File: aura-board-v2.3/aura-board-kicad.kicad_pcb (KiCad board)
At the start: 2 copper layers, 76.8 x 53.3 mm, 21 parts, among them J1 Main Power, J2 PWM_8, J3 BBCON, J4 Atto, J5 GPS, J6 SBUS, J7 Tele, J8 I2C0, U1 TSR2-2450, U2 PocketBeagle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

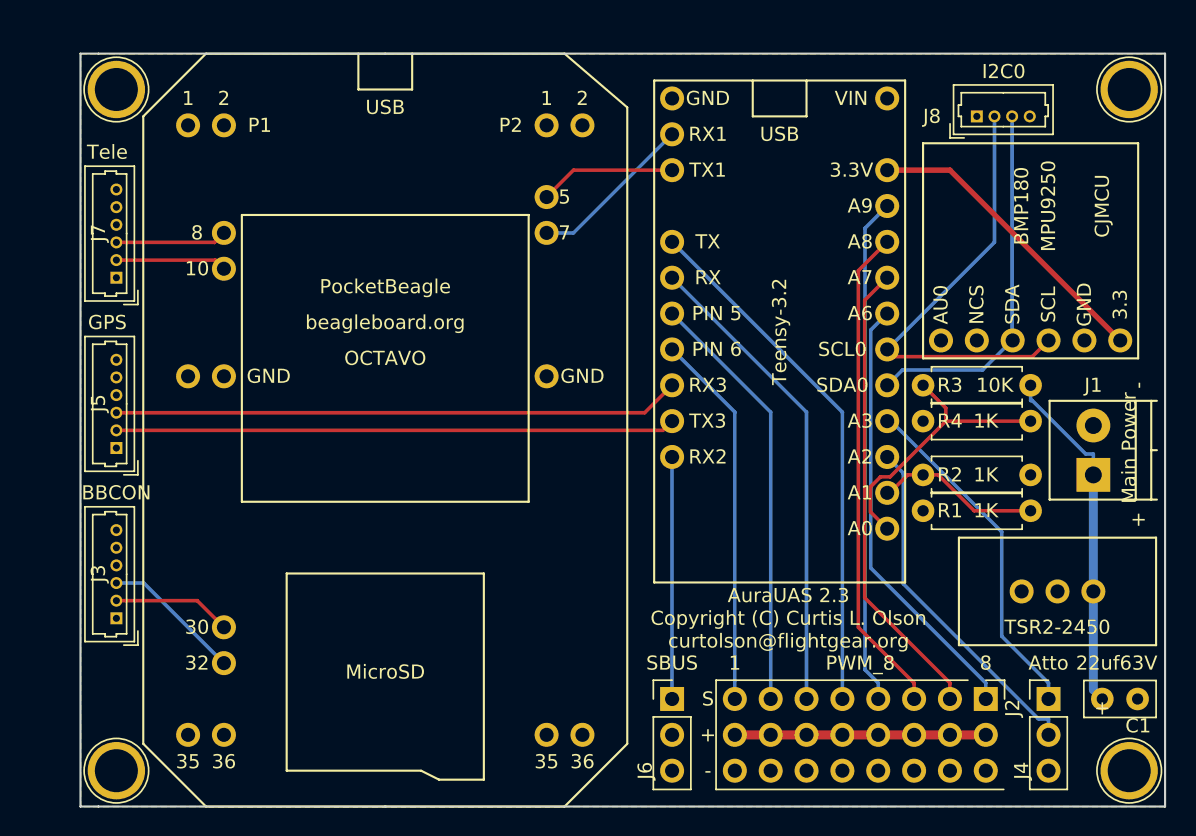
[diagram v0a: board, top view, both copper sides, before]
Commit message: Initial v2.3 design fixes and tweaks: - reverse tx/rx on gps and telemetry (big dohhh!) - slide screw terminal slightly towards board edge - mark pin #1 on TSR2-2450 connector clearly - relocate capacitor - bigger usb port outlines on teensy/pocketbeagle - space sbus and atto connectors exactly 0.2" from ends of PWM block.
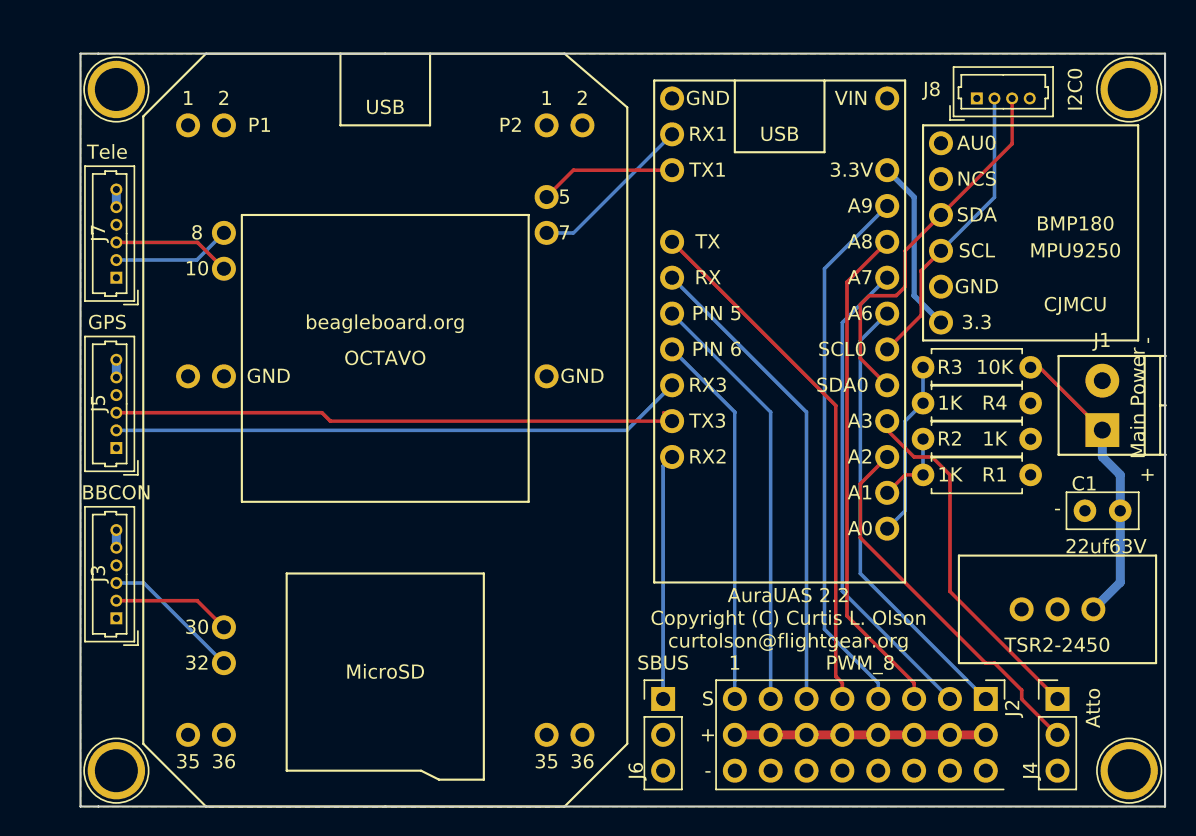
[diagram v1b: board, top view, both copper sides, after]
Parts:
- moved C1 13.4 mm to (101.6, 81.9), turned to 180 degrees
- moved U4 9.92 mm to (95.2, 69.8), turned to 180 degrees
- moved R1 8.03 mm to (87.6, 79.4), turned to 0 degrees
- moved R4 7.73 mm to (95.2, 74.3), turned to 180 degrees
- moved J1 3.24 mm to (100.3, 76.2)
- moved R2 2.54 mm to (95.2, 76.8)
- moved R3 1.27 mm to (87.6, 71.8)
- moved J8 1.27 mm to (91.4, 52.7)
- moved U1 1.27 mm to (97.2, 92.7)
- moved J4 0.64 mm to (97.2, 95.2)
- moved J6 0.63 mm to (69.2, 95.2)
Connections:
- J7 pad 2: /UART2_TX -> /MODEM_TX
- J7 pad 3: /UART2_RX -> /MODEM_RX
- U2 pad 10: /UART2_TX -> /MODEM_RX
- U2 pad 8: /UART2_RX -> /MODEM_TX
- U3 pad 10: /GPS_TX -> /GPS_RX
- U3 pad 9: /GPS_RX -> /GPS_TX
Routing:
- net /I2C0_SCL: track 31.8 -> 20.9 mm
- net +3V3: track 21.5 -> 12.4 mm
- net /MODEM_TX: track 0.00 -> 8.42 mm
- net /MODEM_RX: track 0.00 -> 8.39 mm
- net /UART2_RX: track 7.90 -> 0.00 mm
- net /UART2_TX: track 7.87 -> 0.00 mm
- net /MAIN_VCC: track 19.9 -> 12.5 mm
- net /AVIONICS_VCC: track 11.7 -> 5.61 mm
- net VDD: track 24.7 -> 20.9 mm
- net GND: track 0.00 -> 3.75 mm
- net /PWM5: track 36.0 -> 38.3 mm
- net /ATTO_AMPS: track 24.8 -> 26.6 mm
- net /PWM7: track 33.0 -> 34.3 mm
- net /ATTO_VOLTS: track 24.6 -> 25.7 mm
- net /GPS_TX: track 39.6 -> 40.7 mm
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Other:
- net class Default: clearance 0.1524 -> 0.254
- rule trace_clearance: 0.1524 -> 0.254
- board text added: "AuraUAS 2.2 Copyright (C) Curtis L. Olson curtolson@flightgear.org"
- board text removed: "8"
- board text removed: "AuraUAS 2.3 Copyright (C) Curtis L. Olson curtolson@flightgear.org"

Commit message: Bump up the version number in the board label Fiddle with traces a bit more.
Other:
- board text added: "AuraUAS 2.3 Copyright (C) Curtis L. Olson curtolson@flightgear.org"
- board text removed: "AuraUAS 2.2 Copyright (C) Curtis L. Olson curtolson@flightgear.org"
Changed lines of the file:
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@@
     (area 27.600999 47.993 105.309001 104.459)
     (thickness 1.6)
-    (drawings 14)
+    (drawings 15)
     (tracks 100)
     (zones 0)
@@
   )
   (setup
-    (last_trace_width 0.635)
+    (last_trace_width 0.254)
     (user_trace_width 0.381)
     (user_trace_width 0.508)
@@
       (net 11 +5V))
   )
+  (gr_text 1 (at 101.6 88.9) (layer F.SilkS)
+    (effects (font (size 1 1) (thickness 0.25)))
+  )
   (gr_text - (at 97.155 81.915 180) (layer F.SilkS)
     (effects (font (size 1 1) (thickness 0.25)))
   )
-  (gr_text "AuraUAS 2.2\nCopyright (C) Curtis L. Olson\ncurtolson@flightgear.org" (at 78.105 89.535) (layer F.SilkS)
+  (gr_text "AuraUAS 2.3\nCopyright (C) Curtis L. Olson\ncurtolson@flightgear.org" (at 78.105 89.535) (layer F.SilkS)
     (effects (font (size 1 1) (thickness 0.15)))
   )
@@
   (segment (start 30.48 71.22) (end 30.48 72.47) (width 0.635) (layer B.Cu) (net 2))
   (segment (start 30.48 60.405) (end 30.48 59.155) (width 0.635) (layer B.Cu) (net 2))
-  (segment (start 74.295 74.93) (end 74.295 95.25) (width 0.254) (layer B.Cu) (net 3))
-  (segment (start 69.85 70.485) (end 74.295 74.93) (width 0.254) (layer B.Cu) (net 3))
+  (segment (start 74.295 74.93) (end 74.295 95.25) (width 0.254) (layer B.Cu) (net 3) (status 800000))
+  (segment (start 69.85 70.485) (end 74.295 74.93) (width 0.254) (layer B.Cu) (net 3) (status 400000))
   (segment (start 76.835 74.93) (end 76.835 95.25) (width 0.254) (layer B.Cu) (net 4))
   (segment (start 69.85 67.945) (end 76.835 74.93) (width 0.254) (layer B.Cu) (net 4))
   (segment (start 79.375 74.93) (end 79.375 95.25) (width 0.254) (layer B.Cu) (net 5))
   (segment (start 69.85 65.405) (end 79.375 74.93) (width 0.254) (layer B.Cu) (net 5))
-  (segment (start 81.4469 93.6522) (end 81.915 94.1203) (width 0.254) (layer F.Cu) (net 6))
-  (segment (start 81.4469 74.4619) (end 81.4469 93.6522) (width 0.254) (layer F.Cu) (net 6))
-  (segment (start 69.85 62.865) (end 81.4469 74.4619) (width 0.254) (layer F.Cu) (net 6))
-  (segment (start 81.915 95.25) (end 81.915 94.1203) (width 0.254) (layer F.Cu) (net 6))
+  (segment (start 81.915 95.25) (end 81.915 90.805) (width 0.254) (layer F.Cu) (net 6) (status 400000))
+  (segment (start 81.28 74.295) (end 69.85 62.865) (width 0.254) (layer F.Cu) (net 6) (status 800000))
+  (segment (start 81.28 90.17) (end 81.28 74.295) (width 0.254) (layer F.Cu) (net 6))
+  (segment (start 81.915 90.805) (end 81.28 90.17) (width 0.254) (layer F.Cu) (net 6))
   (segment (start 80.645 90.3103) (end 84.455 94.1203) (width 0.254) (layer B.Cu) (net 7))
   (segment (start 80.645 64.77) (end 80.645 90.3103) (width 0.254) (layer B.Cu) (net 7))

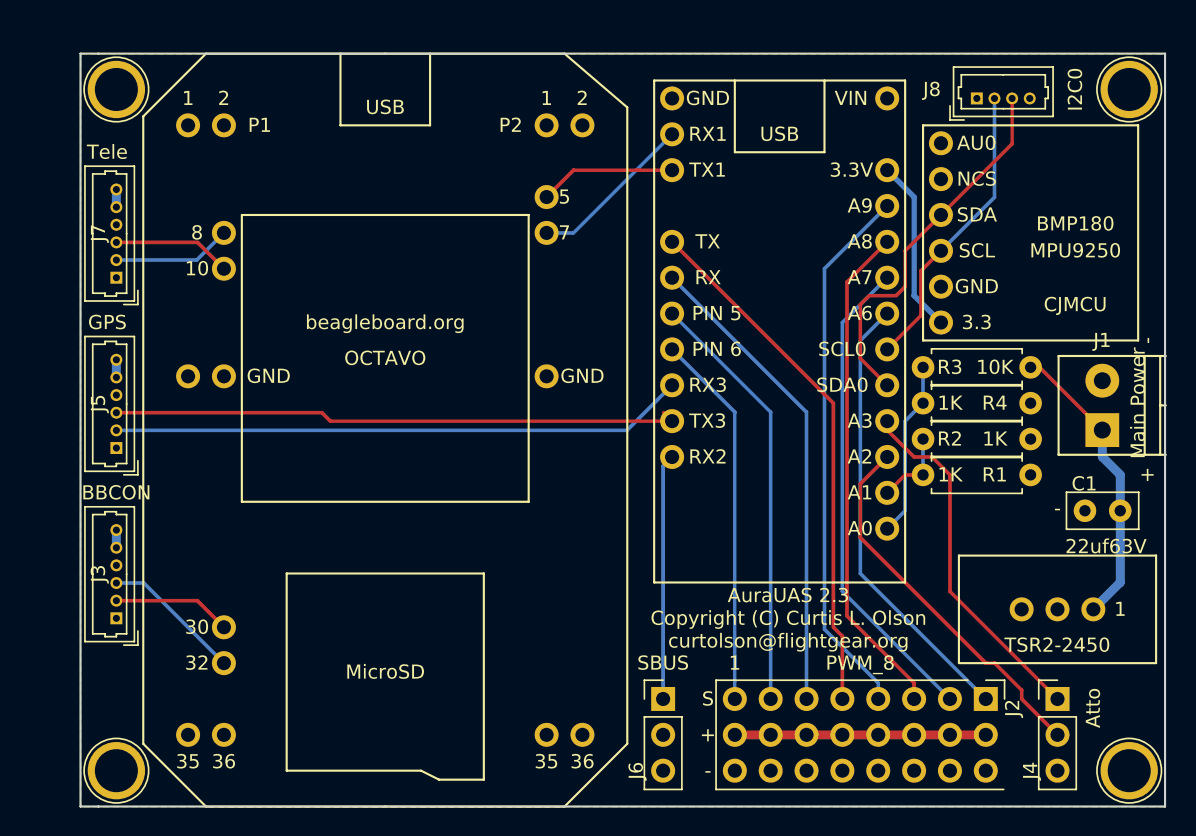
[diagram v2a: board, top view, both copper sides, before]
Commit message: Various small positional adjustments to give better clearance for the upper right mounting hole. Various trace route tweaks for aesthetics.
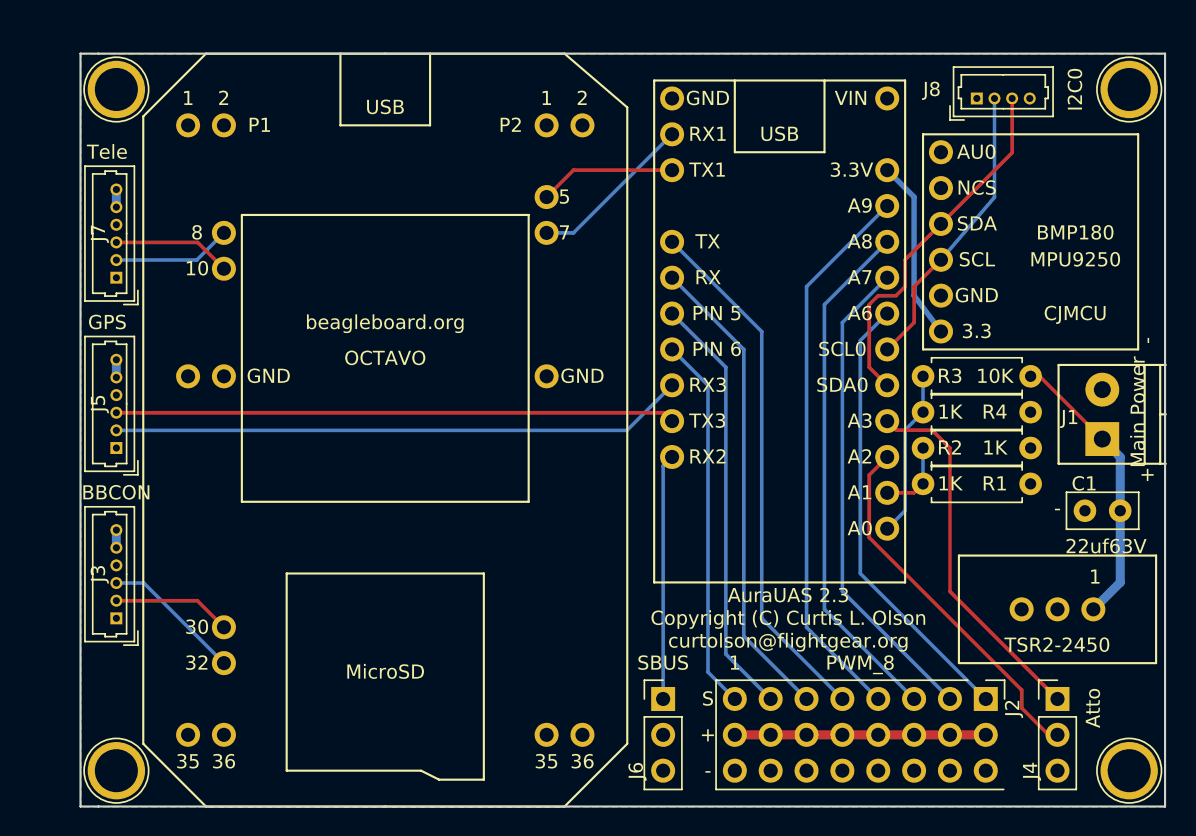
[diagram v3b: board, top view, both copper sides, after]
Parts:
- moved R1 0.64 mm to (87.6, 80.0)
- moved R2 0.64 mm to (95.2, 77.5)
- moved R3 0.64 mm to (87.6, 72.4)
- moved R4 0.64 mm to (95.2, 74.9)
- moved U4 0.64 mm to (95.2, 70.5)
- moved J1 0.63 mm to (100.3, 76.8)
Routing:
- net /ATTO_VOLTS: track 25.7 -> 27.1 mm
- net /PWM6: track 35.5 -> 36.9 mm
- net /PWM5: track 38.3 -> 39.4 mm
- net /I2C0_SDA: track 26.7 -> 25.8 mm
- net VDD: track 20.9 -> 20.3 mm
- net /MAIN_VCC: track 12.5 -> 11.8 mm
- net /ATTO_AMPS: track 26.6 -> 26.1 mm

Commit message: Switch to JST-GH surface mount connectors.
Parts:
- J3, J5, J7: footprint Connectors_Molex:Molex_PicoBlade_53047-0610_06x1.25mm_Straight -> Connectors_JST:JST_GH_BM06B-GHS-TBT_06x1.25mm_Straight
- J8: footprint Connectors_Molex:Molex_PicoBlade_53047-0410_04x1.25mm_Straight -> Connectors_JST:JST_GH_BM04B-GHS-TBT_04x1.25mm_Straight
- moved J7 4.49 mm to (29.8, 61.0)
- moved J8 3.24 mm to (94.6, 53.3)
- moved J3 2.01 mm to (29.8, 91.4)
- moved MH1 1.91 mm to (28.6, 52.1)
- moved MH2 1.91 mm to (28.6, 100.3)
- moved J5 1.42 mm to (29.8, 76.2)
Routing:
- net GND: track 3.75 -> 13.4 mm, vias 0 -> 4
- net /UART0_RX: track 9.97 -> 6.85 mm
- net /I2C0_SDA: track 25.8 -> 27.7 mm, vias 0 -> 1
- net /GPS_RX: track 40.5 -> 38.9 mm
- net /I2C0_SCL: track 20.8 -> 19.5 mm
- net /MODEM_TX: track 8.42 -> 7.73 mm
- net /UART0_TX: track 8.40 -> 7.91 mm, vias 0 -> 1
- net /MODEM_RX: track 8.39 -> 7.90 mm, vias 0 -> 1
- net /GPS_TX: track 40.7 -> 40.4 mm, vias 0 -> 1
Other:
- board size 76.8 x 53.3 mm -> 78.7 x 53.3 mm
